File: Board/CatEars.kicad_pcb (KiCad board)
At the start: 2 copper layers, 65.1 x 39 mm, 52 parts, among them U2 AP2112K-3.3

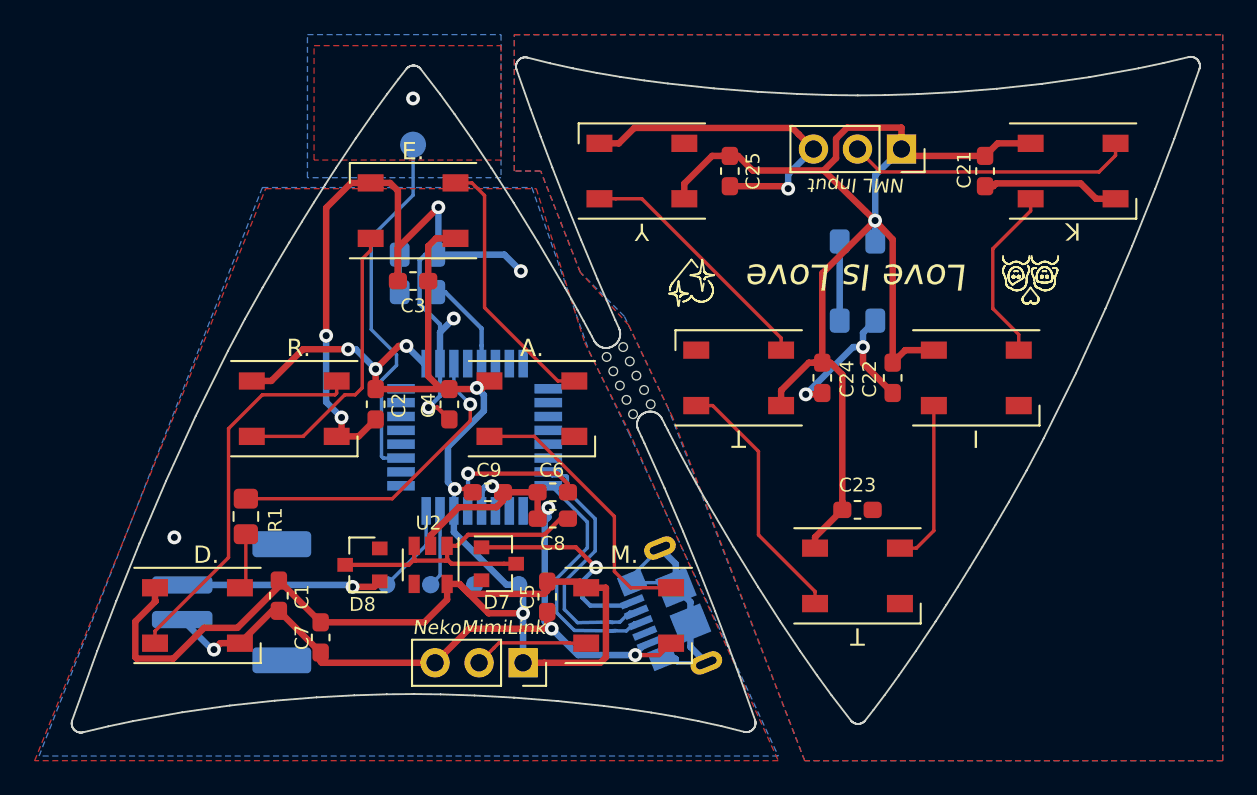
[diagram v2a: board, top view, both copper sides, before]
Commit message: New OSH Park link, rev notes, restored reset
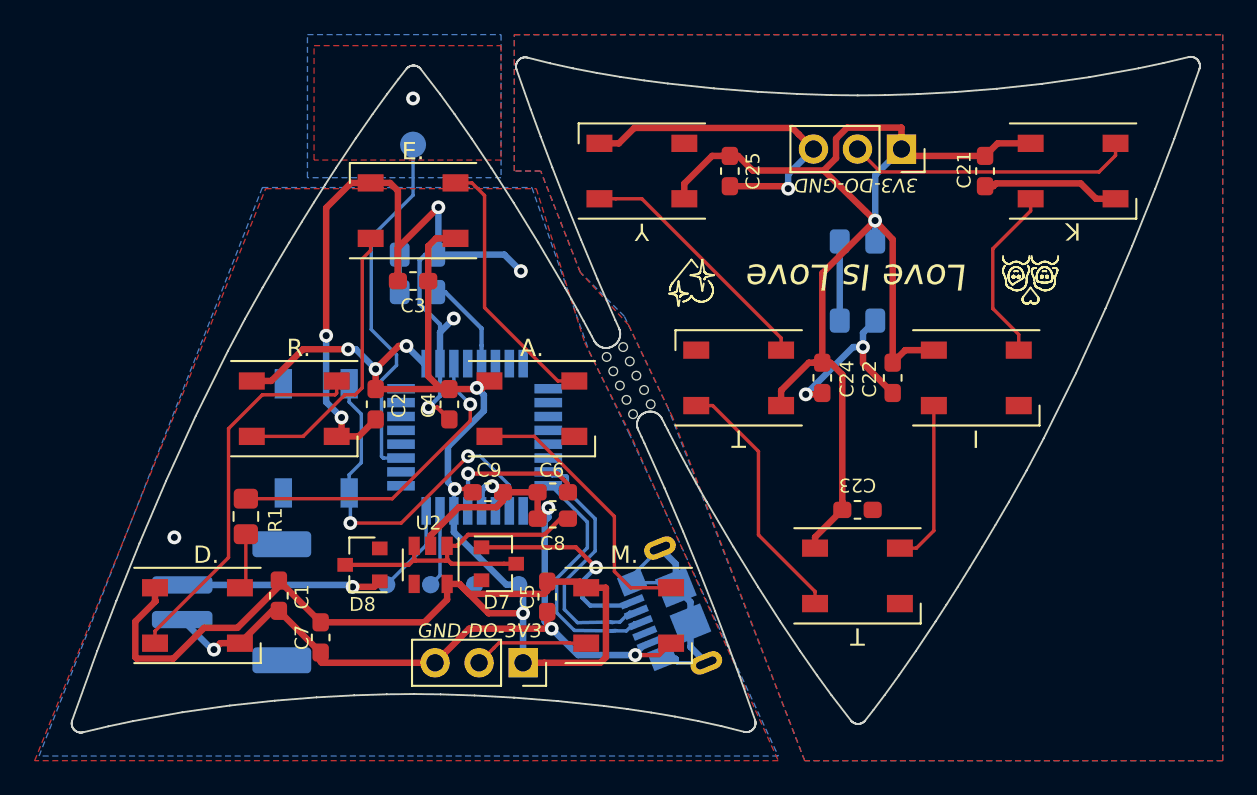
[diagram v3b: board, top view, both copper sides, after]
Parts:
- added Reset: SW_Push, Button_Switch_SMD:SW_SPST_TL3342, B.Cu at (213.1, 137.6)
- 3V3-DO-GND: renamed from NML Input
- renumbered NekoMimiLink to GND-DO-3V3
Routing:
- net Net-(SW1-Pad1): track 0.00 -> 21.6 mm, vias 0 -> 2
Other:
- board text added: "2020 @GalaxyAllieCat"
- board text removed: "Meow Meow Ears v3b by @GalaxyAllieCat 2020-03-02"
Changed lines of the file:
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@@
     (thickness 1.6)
     (drawings 6414)
-    (tracks 367)
+    (tracks 381)
     (zones 0)
-    (modules 52)
+    (modules 53)
     (nets 53)
   )
@@
   )
   (setup
-    (last_trace_width 0.2)
+    (last_trace_width 0.25)
     (user_trace_width 0.2)
     (user_trace_width 0.375)
@@
     (add_net VBUS)
   )
+  (module Button_Switch_SMD:SW_SPST_TL3342 (layer B.Cu)
+    (at 213.106 137.6045 90)
+    (descr "Low-profile SMD Tactile Switch, https://www.e-switch.com/system/asset/product_line/data_sheet/165/TL3342.pdf")
+    (tags "SPST Tactile Switch")
+    (attr smd)
+    (fp_text reference Reset (at 4.826 -0.127 180) (layer B.SilkS)
+      (effects (font (size 0.8 0.8) (thickness 0.15) italic) (justify mirror))
+    )
+    (fp_text value SW_Push (at 0 -3.75 90) (layer B.Fab)
+      (effects (font (size 1 1) (thickness 0.15)) (justify mirror))
+    )
+    (fp_circle (center 0 0) (end 1 0) (layer B.Fab) (width 0.1))
+    (fp_line (start -4.25 -3) (end -4.25 3) (layer B.CrtYd) (width 0.05))
+    (fp_line (start 4.25 -3) (end -4.25 -3) (layer B.CrtYd) (width 0.05))
+    (fp_line (start 4.25 3) (end 4.25 -3) (layer B.CrtYd) (width 0.05))
+    (fp_line (start -4.25 3) (end 4.25 3) (layer B.CrtYd) (width 0.05))
+    (fp_line (start -1.2 2.6) (end -2.6 1.2) (layer B.Fab) (width 0.1))
+    (fp_line (start 1.2 2.6) (end -1.2 2.6) (layer B.Fab) (width 0.1))
+    (fp_line (start 2.6 1.2) (end 1.2 2.6) (layer B.Fab) (width 0.1))
+    (fp_line (start 2.6 -1.2) (end 2.6 1.2) (layer B.Fab) (width 0.1))
+    (fp_line (start 1.2 -2.6) (end 2.6 -1.2) (layer B.Fab) (width 0.1))
+    (fp_line (start -1.2 -2.6) (end 1.2 -2.6) (layer B.Fab) (width 0.1))
+    (fp_line (start -2.6 -1.2) (end -1.2 -2.6) (layer B.Fab) (width 0.1))
+    (fp_line (start -2.6 1.2) (end -2.6 -1.2) (layer B.Fab) (width 0.1))
+    (fp_line (start -1.25 2.75) (end 1.25 2.75) (layer B.SilkS) (width 0.12))
+    (fp_line (start -2.75 1) (end -2.75 -1) (layer B.SilkS) (width 0.12))
+    (fp_line (start -1.25 -2.75) (end 1.25 -2.75) (layer B.SilkS) (width 0.12))
+    (fp_line (start 2.75 1) (end 2.75 -1) (layer B.SilkS) (width 0.12))
+    (fp_line (start -2 -1) (end -2 1) (layer B.Fab) (width 0.1))
+    (fp_line (start -1 -2) (end -2 -1) (layer B.Fab) (width 0.1))
+    (fp_line (start 1 -2) (end -1 -2) (layer B.Fab) (width 0.1))
+    (fp_line (start 2 -1) (end 1 -2) (layer B.Fab) (width 0.1))
+    (fp_line (start 2 1) (end 2 -1) (layer B.Fab) (width 0.1))
+    (fp_line (start 1 2) (end 2 1) (layer B.Fab) (width 0.1))
+    (fp_line (start -1 2) (end 1 2) (layer B.Fab) (width 0.1))
+    (fp_line (start -2 1) (end -1 2) (layer B.Fab) (width 0.1))
+    (fp_line (start -1.7 2.3) (end -1.25 2.75) (layer B.SilkS) (width 0.12))
+    (fp_line (start 1.7 2.3) (end 1.25 2.75) (layer B.SilkS) (width 0.12))
+    (fp_line (start 1.7 -2.3) (end 1.25 -2.75) (layer B.SilkS) (width 0.12))
+    (fp_line (start -1.7 -2.3) (end -1.25 -2.75) (layer B.SilkS) (width 0.12))
+    (fp_line (start 3.2 -1.6) (end 2.2 -1.6) (layer B.Fab) (width 0.1))
+    (fp_line (start 2.7 -2.1) (end 2.7 -1.6) (layer B.Fab) (width 0.1))
+    (fp_line (start 1.7 -2.1) (end 3.2 -2.1) (layer B.Fab) (width 0.1))
+    (fp_line (start -1.7 -2.1) (end -3.2 -2.1) (layer B.Fab) (width 0.1))
+    (fp_line (start -3.2 -1.6) (end -2.2 -1.6) (layer B.Fab) (width 0.1))
+    (fp_line (start -2.7 -2.1) (end -2.7 -1.6) (layer B.Fab) (width 0.1))
+    (fp_line (start -3.2 1.6) (end -2.2 1.6) (layer B.Fab) (width 0.1))
+    (fp_line (start -1.7 2.1) (end -3.2 2.1) (layer B.Fab) (width 0.1))
+    (fp_line (start -2.7 2.1) (end -2.7 1.6) (layer B.Fab) (width 0.1))
+    (fp_line (start 3.2 1.6) (end 2.2 1.6) (layer B.Fab) (width 0.1))
+    (fp_line (start 1.7 2.1) (end 3.2 2.1) (layer B.Fab) (width 0.1))
+    (fp_line (start 2.7 2.1) (end 2.7 1.6) (layer B.Fab) (width 0.1))
+    (fp_line (start -3.2 2.1) (end -3.2 1.6) (layer B.Fab) (width 0.1))
+    (fp_line (start -3.2 -2.1) (end -3.2 -1.6) (layer B.Fab) (width 0.1))
+    (fp_line (start 3.2 2.1) (end 3.2 1.6) (layer B.Fab) (width 0.1))
+    (fp_line (start 3.2 -2.1) (end 3.2 -1.6) (layer B.Fab) (width 0.1))
+    (fp_text user %R (at 0 3.75 90) (layer B.Fab)
+      (effects (font (size 1 1) (thickness 0.15)) (justify mirror))
+    )
+    (pad 2 smd rect (at 3.15 -1.9 90) (size 1.7 1) (layers B.Cu B.Paste B.Mask)
+      (net 1 GND))
+    (pad 2 smd rect (at -3.15 -1.9 90) (size 1.7 1) (layers B.Cu B.Paste B.Mask)
+      (net 1 GND))
+    (pad 1 smd rect (at 3.15 1.9 90) (size 1.7 1) (layers B.Cu B.Paste B.Mask)
+      (net 10 "Net-(SW1-Pad1)"))
+    (pad 1 smd rect (at -3.15 1.9 90) (size 1.7 1) (layers B.Cu B.Paste B.Mask)
+      (net 10 "Net-(SW1-Pad1)"))
+    (model ${KISYS3DMOD}/Button_Switch_SMD.3dshapes/SW_SPST_TL3342.wrl
+      (at (xyz 0 0 0))
+      (scale (xyz 1 1 1))
+      (rotate (xyz 0 0 0))
+    )
+  )
   (module footprints:1mm_npth (layer F.Cu)
     (at 232.41 135.636)
@@
     (descr "Through hole straight socket strip, 1x03, 2.54mm pitch, single row (from Kicad 4.0.7), script generated")
     (tags "Through hole socket strip THT 1x03 2.54mm single row")
-    (fp_text reference "NML Input" (at 2.0828 2.5908 180 unlocked) (layer F.SilkS)
+    (fp_text reference 3V3-DO-GND (at 2.0828 2.5908 180 unlocked) (layer F.SilkS)
       (effects (font (size 0.8 0.8) (thickness 0.15) italic))
     )
@@
     (tags "capacitor handsolder")
     (attr smd)
-    (fp_text reference C23 (at 0 -1.43) (layer F.SilkS)
+    (fp_text reference C23 (at 0 -1.43 180 unlocked) (layer F.SilkS)
       (effects (font (size 0.8 0.8) (thickness 0.15)))
     )
@@
     (descr "Through hole straight socket strip, 1x03, 2.54mm pitch, single row (from Kicad 4.0.7), script generated")
     (tags "Through hole socket strip THT 1x03 2.54mm single row")
-    (fp_text reference NekoMimiLink (at -2.032 2.54 180) (layer F.SilkS)
+    (fp_text reference GND-DO-3V3 (at -1.8415 2.54 180) (layer F.SilkS)
       (effects (font (size 0.8 0.8) (thickness 0.15) italic))
     )
@@
   (gr_line (start 253.724214 129.038497) (end 253.702066 129.044269) (layer F.SilkS) (width 0.105833))
   (gr_line (start 253.746 129.032) (end 253.724214 129.038497) (layer F.SilkS) (width 0.105833))
-  (gr_text "Meow Meow Ears v3b\nby @GalaxyAllieCat\n2020-03-02" (at 212.344 132.08 60) (layer B.SilkS)
+  (gr_text "2020 @GalaxyAllieCat" (at 211.836 128.9685 60) (layer B.SilkS)
     (effects (font (size 1 1) (thickness 0.15) italic) (justify mirror))
   )
-  (gr_text 3.3-6V (at 212.1535 141.224) (layer B.SilkS)
+  (gr_text 3.3-6V (at 213.995 147.193 90) (layer B.SilkS)
     (effects (font (size 0.8 0.8) (thickness 0.15)) (justify mirror))
   )
@@
   (segment (start 221.05 134.69) (end 221.05 133.291) (width 0.2) (layer B.Cu) (net 9))
   (segment (start 221.996 135.636) (end 221.05 134.69) (width 0.2) (layer B.Cu) (net 9))
+  (segment (start 215.006 139.7045) (end 215.006 140.7545) (width 0.2) (layer B.Cu) (net 10))
+  (segment (start 215.706 139.0045) (end 215.006 139.7045) (width 0.2) (layer B.Cu) (net 10))
+  (segment (start 215.706 136.2045) (end 215.706 139.0045) (width 0.2) (layer B.Cu) (net 10))
+  (segment (start 215.006 134.4545) (end 215.006 135.5045) (width 0.2) (layer B.Cu) (net 10))
+  (segment (start 215.006 135.5045) (end 215.706 136.2045) (width 0.2) (layer B.Cu) (net 10))
+  (via (at 221.869 138.636497) (size 0.8) (drill 0.4) (layers F.Cu B.Cu) (net 10))
+  (segment (start 222.576999 138.636497) (end 221.869 138.636497) (width 0.2) (layer B.Cu) (net 10))
+  (segment (start 224.25 141.791) (end 224.25 140.309498) (width 0.2) (layer B.Cu) (net 10))
+  (segment (start 224.25 140.309498) (end 222.576999 138.636497) (width 0.2) (layer B.Cu) (net 10))
+  (via (at 215.0745 142.494) (size 0.8) (drill 0.4) (layers F.Cu B.Cu) (net 10))
+  (segment (start 221.869 138.636497) (end 218.011497 142.494) (width 0.2) (layer F.Cu) (net 10))
+  (segment (start 218.011497 142.494) (end 215.0745 142.494) (width 0.2) (layer F.Cu) (net 10))
+  (segment (start 215.0745 140.823) (end 215.006 140.7545) (width 0.2) (layer B.Cu) (net 10))
+  (segment (start 215.0745 142.494) (end 215.0745 140.823) (width 0.2) (layer B.Cu) (net 10))
   (segment (start 226.663603 140.341) (end 228.756 142.433397) (width 0.2) (layer B.Cu) (net 28))
   (segment (start 226.5 140.341) (end 226.663603 140.341) (width 0.2) (layer B.Cu) (net 28))
